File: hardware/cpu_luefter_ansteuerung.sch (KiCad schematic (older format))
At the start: 26 parts, among them IC1 ATMEGA8A-A, P1 POWER 12V DC, P2 ISP, P3 CPU LUEFTER, Q1 BC817-40, SW1 SW_PUSH, U1 7805, U2 CD4543, Y1 Crystal 12MHz

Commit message: Portierung zu KiCad 5.1.2
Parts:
- removed C1, C8: 100u, Capacitors_SMD:c_elec_6.3x5.7, symbol CP
- removed C10, C2, C4, C6, C7: 100n, Capacitors_SMD:C_0805_HandSoldering, symbol C
- removed C3, C5: 22p, Capacitors_SMD:C_0805_HandSoldering, symbol C
- removed C9: 1u, Capacitors_SMD:C_0805_HandSoldering, symbol C
- removed D1, D2: 1N4001, Diodes_SMD:SMA_Handsoldering, symbol D
- removed IC1: ATMEGA8A-A, Housings_QFP:TQFP-32_7x7mm_Pitch0.8mm, symbol ATMEGA8A-A
- removed P1: POWER 12V DC, Pin_Headers:Pin_Header_Straight_1x02, symbol CONN_01X02
- removed P2: ISP, Pin_Headers:Pin_Header_Straight_2x03, symbol CONN_02X03
- removed P3: CPU LUEFTER, Pin_Headers:Pin_Header_Straight_1x04, symbol CONN_01X04
- removed Q1: BC817-40, TO_SOT_Packages_SMD:SOT-23_Handsoldering, symbol BC817-40
- removed R1, R2, R3: 10k, Resistors_SMD:R_0805_HandSoldering, symbol R
- removed R4: 220, Resistors_SMD:R_0805_HandSoldering, symbol R
- removed SW1: SW_PUSH, Buttons_Switches_ThroughHole:SW_PUSH_SMALL, symbol SW_PUSH
- removed U2: CD4543, SMD_Packages:SO-16-N, symbol CD4543
- removed Y1: Crystal 12MHz, Crystals:Crystal_HC49-SD_SMD, symbol Crystal
- added C1, C7: 100u, Capacitor_THT:CP_Radial_D4.0mm_P1.50mm, symbol Device:CP
- added C2, C4: 22p, Capacitor_THT:C_Disc_D7.0mm_W2.5mm_P5.00mm, symbol Device:C
- added C3, C5, C6: 100n, Capacitor_THT:C_Disc_D5.0mm_W2.5mm_P2.50mm, symbol Device:C
- added C8: 1u, Capacitor_THT:CP_Radial_D10.0mm_P2.50mm_P5.00mm, symbol Device:CP
- added C9: 100n, Capacitor_THT:CP_Radial_D10.0mm_P2.50mm, symbol Device:C
- added D1, D2: 1N4001, Diode_THT:D_DO-41_SOD81_P10.16mm_Horizontal, symbol Diode:1N4001
- added J1: Power 12V DC, Connector_Molex:Molex_KK-254_AE-6410-02A_1x02_P2.54mm_Vertical, symbol Connector_Generic:Conn_01x02
- added J2: ISP, Connector_IDC:IDC-Header_2x03_P2.54mm_Vertical, symbol Connector_Generic:Conn_02x03_Odd_Even
- added J3: CPU Lüfter, Connector_PinHeader_1.27mm:PinHeader_1x04_P1.27mm_Vertical, symbol Connector_Generic:Conn_01x04
- added Q1: BC337, Package_TO_SOT_THT:TO-92_Inline, symbol Transistor_BJT:BC337
- added R1, R2, R3: 10k, Resistor_THT:R_Axial_DIN0207_L6.3mm_D2.5mm_P10.16mm_Horizontal, symbol Device:R
- added R4: 220, Resistor_THT:R_Axial_DIN0207_L6.3mm_D2.5mm_P10.16mm_Horizontal, symbol Device:R
- added SW1: SW_Push, Button_Switch_THT:SW_PUSH_6mm_H5mm, symbol Switch:SW_Push
- added U2: ATmega8-16PU, Package_DIP:DIP-28_W7.62mm_LongPads, symbol MCU_Microchip_ATmega:ATmega8-16PU
- added U3: 4543, Package_DIP:DIP-16_W7.62mm_LongPads, symbol 4xxx_IEEE:4543
- added Y1: Crystal 12MHz, Crystal:Crystal_HC49-4H_Vertical, symbol Device:Crystal
- AFF1: footprint Displays_7-Segment:7SegmentLED_LTS6760_LTS6780 -> Display_7Segment:7SegmentLED_LTS6760_LTS6780; symbol 7SEGMENTS -> Display_Character:HDSP-A151
- U1: footprint TO_SOT_Packages_SMD:SOT-404 -> Package_TO_SOT_THT:TO-220-3_Horizontal_TabDown; symbol 7805-RESCUE-cpu_luefter_ansteuerung -> Regulator_Linear:L78L05_TO92
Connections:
- wire segments 121 -> 140
- no-connect marks 13 -> 11

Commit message: Hardware auf ATiny24A umgestellt und statt 4543 jetzt ein Leistungs Shiftregister für 7Segment ansteuerung.
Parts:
- removed AFF1: 7SEGMENTS, Display_7Segment:7SegmentLED_LTS6760_LTS6780, symbol Display_Character:HDSP-A151
- removed C1, C7: 100u, Capacitor_THT:CP_Radial_D4.0mm_P1.50mm, symbol Device:CP
- removed C4: 22p, Capacitor_THT:C_Disc_D7.0mm_W2.5mm_P5.00mm, symbol Device:C
- removed C6: 100n, Capacitor_THT:C_Disc_D5.0mm_W2.5mm_P2.50mm, symbol Device:C
- removed C9: 100n, Capacitor_THT:CP_Radial_D10.0mm_P2.50mm, symbol Device:C
- removed D1: 1N4001, Diode_THT:D_DO-41_SOD81_P10.16mm_Horizontal, symbol Diode:1N4001
- removed R3: 10k, Resistor_THT:R_Axial_DIN0207_L6.3mm_D2.5mm_P10.16mm_Horizontal, symbol Device:R
- removed U2: ATmega8-16PU, Package_DIP:DIP-28_W7.62mm_LongPads, symbol MCU_Microchip_ATmega:ATmega8-16PU
- removed U3: 4543, Package_DIP:DIP-16_W7.62mm_LongPads, symbol 4xxx_IEEE:4543
- removed Y1: Crystal 12MHz, Crystal:Crystal_HC49-4H_Vertical, symbol Device:Crystal
- added C1: 100n, Capacitor_THT:C_Disc_D5.0mm_W2.5mm_P2.50mm, symbol Device:C
- added R10, R2, R3, R4, R6, R7, R8, R9: 150, symbol cpu_luefter_ansteuerung-rescue:R
- added U1: ATtiny24A-PU, Package_DIP:DIP-14_W7.62mm, symbol MCU_Microchip_ATtiny:ATtiny24A-PU
- added U2: KCSA02-123, Display_7Segment:KCSC02-123, symbol Display_Character:KCSA02-123
- added U3: TPIC6595, symbol Interface_Expansion:TPIC6595
- C2: value 22p -> 100n; footprint Capacitor_THT:C_Disc_D7.0mm_W2.5mm_P5.00mm -> Capacitor_THT:C_Disc_D5.0mm_W2.5mm_P2.50mm
- C4: renamed from C3; value 100n -> 0,33u
- C5: value 100n -> 0,1u
- renumbered C8 to C3, D2 to D1, J2 to J1, J3 to J2, J1 to J3, R4 to R1, R2 to R11, R1 to R5, U1 to U4
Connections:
- wire segments 140 -> 107
- no-connect marks 11 -> 4
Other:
- note added: "Stützkondensatoren\nU1, U3"
- moved on the sheet: C3, C4, C5, D1, J1, J2, Q1, R1, R11, R5, SW1

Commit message: Schaltplan etwas optimiert -> Rev: 2.1
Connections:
- net PUSH_BUTTON1: now reaches C3.1, R11.1, SW1.1
- net PUSH_BUTTON1: now also U1.2 (XTAL1/PB0); no longer U1.11 (PA2)
- net 7_SEG_SRCK: now reaches U1.12 (PA1)
- net 7_SEG_SRCK: now also U3.13 (SRCK); no longer J2.4 (Pin_4)
- net 7_SEG_SER: now reaches U1.13 (AREF/PA0)
- net 7_SEG_SER: now also U3.3 (SER_IN); no longer R1.2
- net FAN_POWER: now reaches U1.3 (XTAL2/PB1)
- net FAN_POWER: now also R1.2; no longer U3.13 (SRCK)
- net RESET: now reaches J1.5 (Pin_5), R5.2, U1.4 (~RESET~/PB3)
- net 7_SEG_RCLK: now reaches U3.12 (RCLK)
- net 7_SEG_RCLK: now also U1.11 (PA2); no longer U1.5 (PB2)
- net MOSI: now reaches J1.4 (Pin_4), U1.7 (PA6)
- net MISO: now reaches J1.1 (Pin_1), U1.8 (PA5)
- net SCK: now reaches J1.3 (Pin_3), U1.9 (PA4)
- new net FAN_PWM: J2.4 (Pin_4), U1.5 (PB2)
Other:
- note added: "7 Segment Anzeige"
- note added: "ISP Schnittstelle"
- note added: "Lüfteransteuerung"
- note added: "Microkontroller Attiny24a"
- moved on the sheet: C3, D1, J1, J2, Q1, R1, R10, R11, R2, R3, R4, R5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

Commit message: Schaltplan optimiert -> Rev: 2.2 TPIC6B595 durch 74HC595 ersetzt. Alle Bauteile Footprints zugewiesen.
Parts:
- removed U3: TPIC6595, symbol Interface_Expansion:TPIC6595
- added U3: 74HC595, Package_DIP:DIP-16_W7.62mm_LongPads, symbol 74xx:74HC595
- R10: renamed from R9; footprint (none) -> Resistor_THT:R_Axial_DIN0207_L6.3mm_D2.5mm_P10.16mm_Horizontal
- R11: renamed from R10; footprint (none) -> Resistor_THT:R_Axial_DIN0207_L6.3mm_D2.5mm_P10.16mm_Horizontal
- R4: renamed from R2; footprint (none) -> Resistor_THT:R_Axial_DIN0207_L6.3mm_D2.5mm_P10.16mm_Horizontal
- R5: renamed from R3; footprint (none) -> Resistor_THT:R_Axial_DIN0207_L6.3mm_D2.5mm_P10.16mm_Horizontal
- R6: renamed from R4; footprint (none) -> Resistor_THT:R_Axial_DIN0207_L6.3mm_D2.5mm_P10.16mm_Horizontal
- R7: renamed from R6; footprint (none) -> Resistor_THT:R_Axial_DIN0207_L6.3mm_D2.5mm_P10.16mm_Horizontal
- R8: renamed from R7; footprint (none) -> Resistor_THT:R_Axial_DIN0207_L6.3mm_D2.5mm_P10.16mm_Horizontal
- R9: renamed from R8; footprint (none) -> Resistor_THT:R_Axial_DIN0207_L6.3mm_D2.5mm_P10.16mm_Horizontal
- U4: renamed from U2; footprint Display_7Segment:KCSC02-123 -> Display_7Segment:HDSP-7801
- renumbered C4 to C3, C5 to C4, C3 to C5, J3 to J1, J1 to J2, J2 to J3, R11 to R1, R5 to R2, R1 to R3, U4 to U1, U1 to U2
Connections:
- net +5V: now also U3.10 (~SRCLR), U3.16 (VCC)
- net 7_SEG_RCLK: now also U3.12 (RCLK)
- net 7_SEG_SER: now also U3.14 (SER)
- net 7_SEG_SRCK: now also U3.11 (SRCLK)
- net GND: now also U3.13 (~OE), U3.8 (GND)
- net at R8.2: now also U3.4 (QE)
- net at R9.2: now also U3.5 (QF)
- net at R10.2: now also U3.6 (QG)
- net at R11.2: now also U3.7 (QH)
- net at R4.2: now also U3.15 (QA)
- net at R5.2: now also U3.1 (QB)
- net at R6.2: now also U3.2 (QC)
- net at R7.2: now also U3.3 (QD)

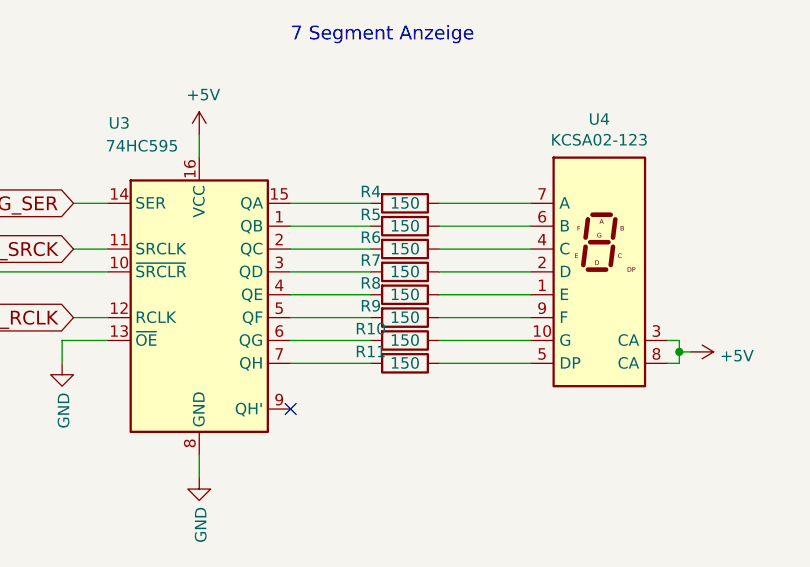
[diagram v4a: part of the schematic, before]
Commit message: Vorwiderstaende fuer 7Segment Anzeige von 150 Ohm auf 560 Ohm geaendert. 74HC595 darf nur gesammt 70mA treiben.
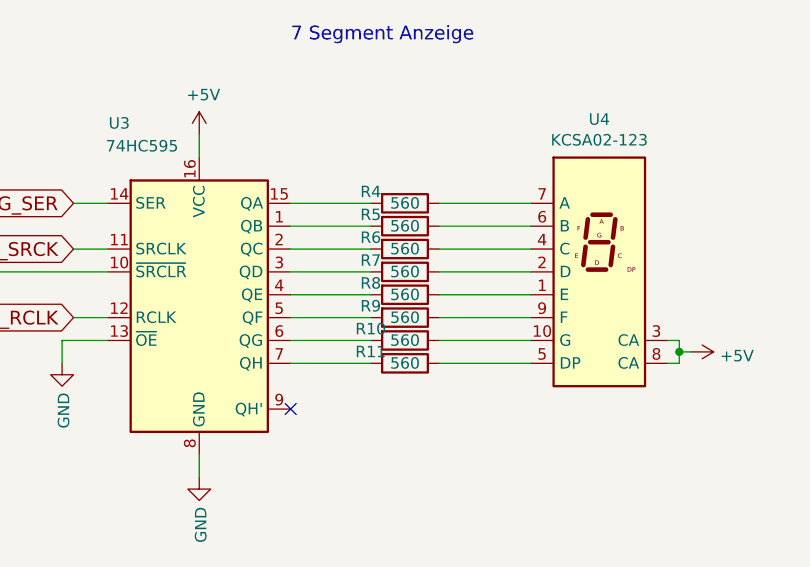
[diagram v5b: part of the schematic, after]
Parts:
- R10, R11, R4, R5, R6, R7, R8, R9: value 150 -> 560
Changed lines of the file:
@@
 Sheet 1 1
 Title "Lüftersteuerung"
-Date "2019-05-15"
-Rev "2.2"
+Date "2019-05-17"
+Rev "2.3"
 Comp "Thorsten Kattanek"
 Comment1 ""
@@
 P 8750 2700
 F 0 "R11" V 8700 2550 50  0000 C CNN
-F 1 "150" V 8750 2700 50  0000 C CNN
+F 1 "560" V 8750 2700 50  0000 C CNN
 F 2 "Resistor_THT:R_Axial_DIN0207_L6.3mm_D2.5mm_P10.16mm_Horizontal" V 8680 2700 50  0001 C CNN
 F 3 "" H 8750 2700 50  0000 C CNN
@@
 P 8750 2600
 F 0 "R10" V 8700 2450 50  0000 C CNN
-F 1 "150" V 8750 2600 50  0000 C CNN
+F 1 "560" V 8750 2600 50  0000 C CNN
 F 2 "Resistor_THT:R_Axial_DIN0207_L6.3mm_D2.5mm_P10.16mm_Horizontal" V 8680 2600 50  0001 C CNN
 F 3 "" H 8750 2600 50  0000 C CNN
@@
 P 8750 2500
 F 0 "R9" V 8700 2350 50  0000 C CNN
-F 1 "150" V 8750 2500 50  0000 C CNN
+F 1 "560" V 8750 2500 50  0000 C CNN
 F 2 "Resistor_THT:R_Axial_DIN0207_L6.3mm_D2.5mm_P10.16mm_Horizontal" V 8680 2500 50  0001 C CNN
 F 3 "" H 8750 2500 50  0000 C CNN
@@
 P 8750 2400
 F 0 "R8" V 8700 2250 50  0000 C CNN
-F 1 "150" V 8750 2400 50  0000 C CNN
+F 1 "560" V 8750 2400 50  0000 C CNN
 F 2 "Resistor_THT:R_Axial_DIN0207_L6.3mm_D2.5mm_P10.16mm_Horizontal" V 8680 2400 50  0001 C CNN
 F 3 "" H 8750 2400 50  0000 C CNN
@@
 P 8750 2300
 F 0 "R7" V 8700 2150 50  0000 C CNN
-F 1 "150" V 8750 2300 50  0000 C CNN
+F 1 "560" V 8750 2300 50  0000 C CNN
 F 2 "Resistor_THT:R_Axial_DIN0207_L6.3mm_D2.5mm_P10.16mm_Horizontal" V 8680 2300 50  0001 C CNN
 F 3 "" H 8750 2300 50  0000 C CNN
@@
 P 8750 2200
 F 0 "R6" V 8700 2050 50  0000 C CNN
-F 1 "150" V 8750 2200 50  0000 C CNN
+F 1 "560" V 8750 2200 50  0000 C CNN
 F 2 "Resistor_THT:R_Axial_DIN0207_L6.3mm_D2.5mm_P10.16mm_Horizontal" V 8680 2200 50  0001 C CNN
 F 3 "" H 8750 2200 50  0000 C CNN
@@
 P 8750 2100
 F 0 "R5" V 8700 1950 50  0000 C CNN
-F 1 "150" V 8750 2100 50  0000 C CNN
+F 1 "560" V 8750 2100 50  0000 C CNN
 F 2 "Resistor_THT:R_Axial_DIN0207_L6.3mm_D2.5mm_P10.16mm_Horizontal" V 8680 2100 50  0001 C CNN
 F 3 "" H 8750 2100 50  0000 C CNN
@@
 P 8750 2000
 F 0 "R4" V 8700 1850 50  0000 C CNN
-F 1 "150" V 8750 2000 50  0000 C CNN
+F 1 "560" V 8750 2000 50  0000 C CNN
 F 2 "Resistor_THT:R_Axial_DIN0207_L6.3mm_D2.5mm_P10.16mm_Horizontal" V 8680 2000 50  0001 C CNN
 F 3 "" H 8750 2000 50  0000 C CNN

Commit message: Fix im Schaltplan.
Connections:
- net 7_SEG_SRCK renamed 7_SEG_SRCLK
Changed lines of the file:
@@
 7_SEG_SER
 Text GLabel 4650 1850 2    60   Input ~ 0
-7_SEG_SRCK
+7_SEG_SRCLK
 Text GLabel 7300 2200 0    60   Input ~ 0
-7_SEG_SRCK
+7_SEG_SRCLK
 Text GLabel 4650 1950 2    60   Input ~ 0
 7_SEG_RCLK

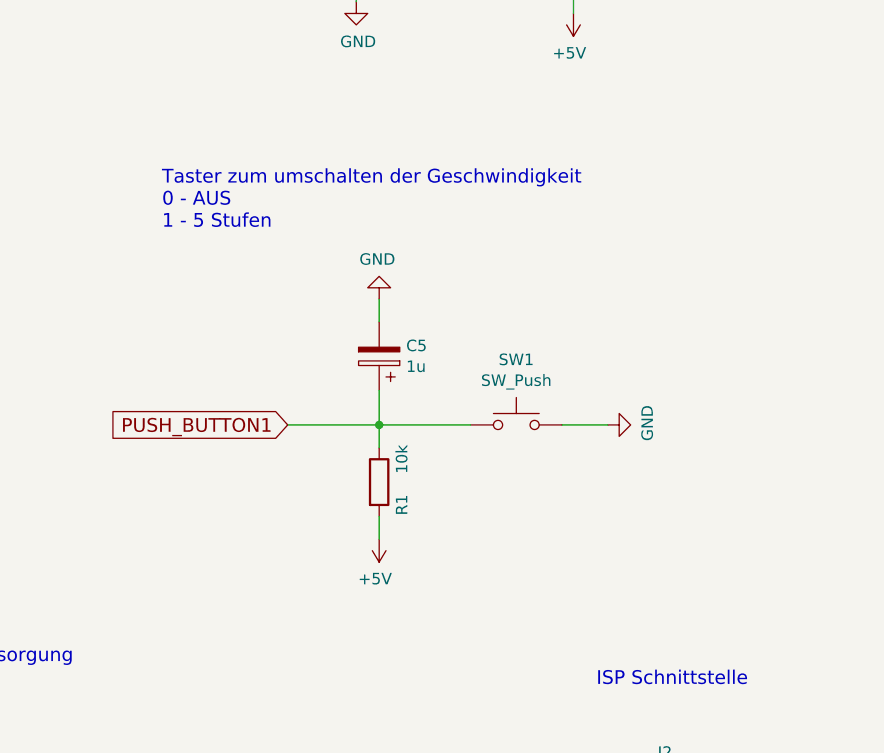
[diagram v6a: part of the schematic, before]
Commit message: Schaltplan an neuer Firmware angepasst.
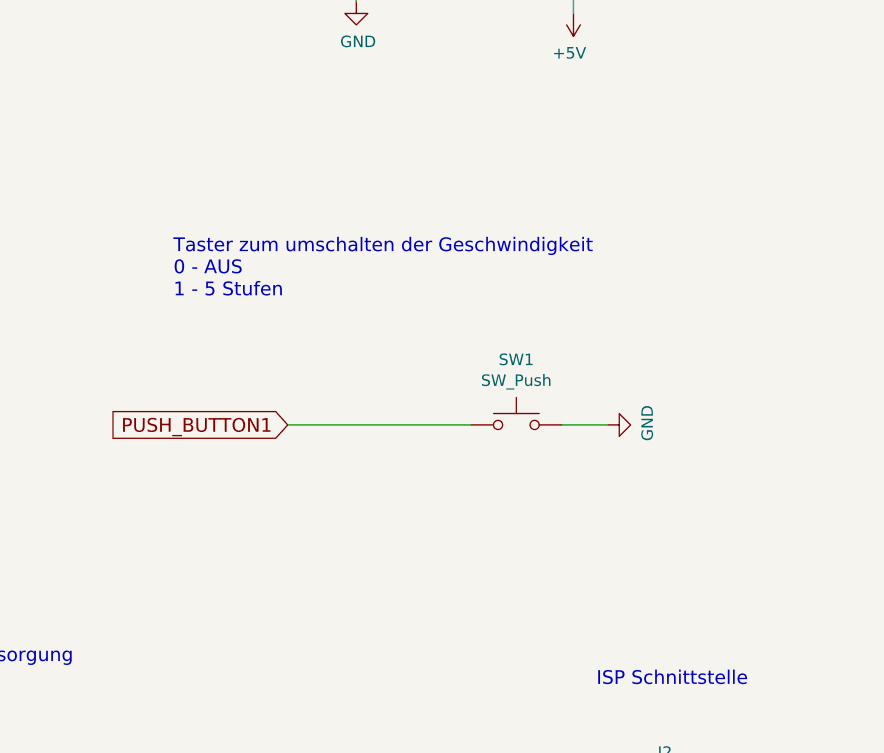
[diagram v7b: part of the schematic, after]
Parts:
- removed C5: 1u, Capacitor_THT:CP_Radial_D10.0mm_P2.50mm_P5.00mm, symbol Device:CP
- removed R1: 10k, Resistor_THT:R_Axial_DIN0207_L6.3mm_D2.5mm_P10.16mm_Horizontal, symbol Device:R
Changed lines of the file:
@@
 Sheet 1 1
 Title "Lüftersteuerung"
-Date "2019-05-17"
-Rev "2.3"
+Date "2019-05-19"
+Rev "2.4"
 Comp "Thorsten Kattanek"
 Comment1 ""
@@
 	8500 5000 8500 5050
 NoConn ~ 9700 5000
-Wire Wire Line
-	3650 5300 4050 5300
-$Comp
-L power:+5V #PWR011
-U 1 1 575F8DD8
-P 4050 5800
-F 0 "#PWR011" H 4050 5650 50  0001 C CNN
-F 1 "+5V" H 4068 5974 50  0000 C CNN
-F 2 "" H 4050 5800 50  0000 C CNN
-F 3 "" H 4050 5800 50  0000 C CNN
-	1    4050 5800
-	-1   0    0    1
-$EndComp
-Wire Wire Line
-	4050 5150 4050 5300
-Wire Wire Line
-	4050 5700 4050 5800
-Connection ~ 4050 5300
 $Comp
 L power:GND #PWR013
@@
 Wire Wire Line
 	4850 5300 5050 5300
-$Comp
-L power:GND #PWR010
-U 1 1 575F940E
-P 4050 4750
-F 0 "#PWR010" H 4050 4500 50  0001 C CNN
-F 1 "GND" H 4058 4576 50  0000 C CNN
-F 2 "" H 4050 4750 50  0000 C CNN
-F 3 "" H 4050 4750 50  0000 C CNN
-	1    4050 4750
-	-1   0    0    1
-$EndComp
-Wire Wire Line
-	4050 4750 4050 4850
-Text Notes 3100 4450 0    60   ~ 0
+Text Notes 3150 4750 0    60   ~ 0
 Taster zum umschalten der Geschwindigkeit\n0 - AUS\n1 - 5 Stufen
 $Comp
@@
 	8800 5050 9050 5050
 Wire Wire Line
-	4050 5300 4450 5300
-Wire Wire Line
-	4050 5300 4050 5400
-Wire Wire Line
 	3950 3250 3950 3450
 $Comp
@@
 	1    2750 7150
 	1    0    0    -1
-$EndComp
-$Comp
-L Device:CP C5
-U 1 1 5CE4D188
-P 4050 5000
-F 0 "C5" H 3932 4954 50  0000 R CNN
-F 1 "1u" H 3932 5045 50  0000 R CNN
-F 2 "Capacitor_THT:CP_Radial_D10.0mm_P2.50mm_P5.00mm" H 4088 4850 50  0001 C CNN
-F 3 "~" H 4050 5000 50  0001 C CNN
-	1    4050 5000
-	-1   0    0    1
 $EndComp
 $Comp
@@
 	1    8200 5350
 	0    1    1    0
-$EndComp
-$Comp
-L Device:R R1
-U 1 1 5D0A41DB
-P 4050 5550
-F 0 "R1" V 4150 5450 50  0000 C CNN
-F 1 "10k" V 4150 5650 50  0000 C CNN
-F 2 "Resistor_THT:R_Axial_DIN0207_L6.3mm_D2.5mm_P10.16mm_Horizontal" V 3980 5550 50  0001 C CNN
-F 3 "~" H 4050 5550 50  0001 C CNN
-	1    4050 5550
-	1    0    0    -1
 $EndComp
 $Comp
@@
 	1    0    0    -1
 $EndComp
+Wire Wire Line
+	3650 5300 4450 5300
 $EndSCHEMATC

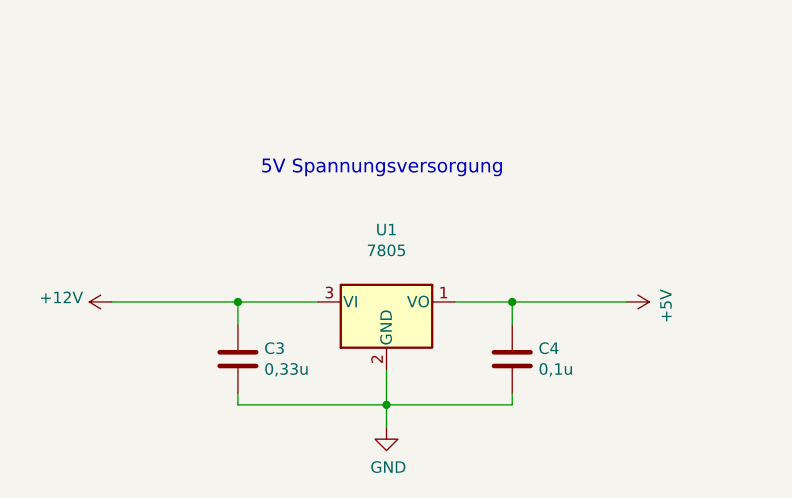
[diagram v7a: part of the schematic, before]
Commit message: Shematic und PCB für 7805 korrigiert. Neue Gerber Dateien erzeugt
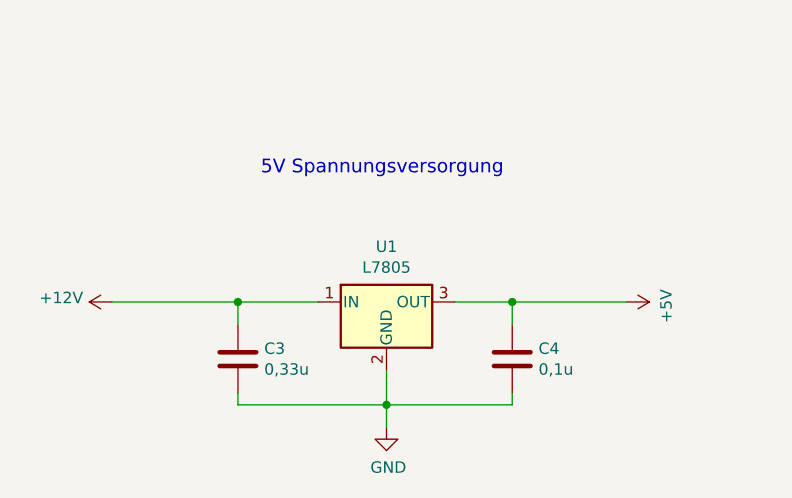
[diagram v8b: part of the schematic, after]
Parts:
- removed U1: 7805, Package_TO_SOT_THT:TO-220-3_Horizontal_TabDown, symbol Regulator_Linear:L78L05_TO92
- added U1: L7805, Package_TO_SOT_THT:TO-220-3_Horizontal_TabDown, symbol Regulator_Linear:L7805
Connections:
- net +12V: now also U1.1 (IN)
- net +5V: now also U1.3 (OUT)
- net GND: now also U1.2 (GND)
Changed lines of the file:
@@
 Sheet 1 1
 Title "Lüftersteuerung"
-Date "2019-05-19"
-Rev "2.4"
+Date "2019-06-20"
+Rev "2.5"
 Comp "Thorsten Kattanek"
 Comment1 ""
@@
 	2500 6900 2750 6900
 Wire Wire Line
-	2200 7200 2200 7350
-Wire Wire Line
 	2750 7350 2750 7300
 Connection ~ 2200 7350
@@
 	1    3250 6900
 	0    1    1    0
-$EndComp
-$Comp
-L Regulator_Linear:L78L05_TO92 U1
-U 1 1 5761B641
-P 2200 6900
-F 0 "U1" H 2200 7215 50  0000 C CNN
-F 1 "7805" H 2200 7124 50  0000 C CNN
-F 2 "Package_TO_SOT_THT:TO-220-3_Horizontal_TabDown" H 2200 6900 50  0001 C CNN
-F 3 "" H 2200 6900 50  0000 C CNN
-	1    2200 6900
-	1    0    0    -1
 $EndComp
 Text Notes 10100 4800 0    60   ~ 0
@@
 Wire Wire Line
 	3650 5300 4450 5300
+$Comp
+L Regulator_Linear:L7805 U1
+U 1 1 5D0DDDB7
+P 2200 6900
+F 0 "U1" H 2200 7142 50  0000 C CNN
+F 1 "L7805" H 2200 7051 50  0000 C CNN
+F 2 "Package_TO_SOT_THT:TO-220-3_Horizontal_TabDown" H 2225 6750 50  0001 L CIN
+F 3 "http://www.st.com/content/ccc/resource/technical/document/datasheet/41/4f/b3/b0/12/d4/47/88/CD00000444.pdf/files/CD00000444.pdf/jcr:content/translations/en.CD00000444.pdf" H 2200 6850 50  0001 C CNN
+	1    2200 6900
+	1    0    0    -1
+$EndComp
+Wire Wire Line
+	2200 7200 2200 7350
 $EndSCHEMATC
